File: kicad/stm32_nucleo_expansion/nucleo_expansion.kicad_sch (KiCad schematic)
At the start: 51 parts, among them CN10 NUCLE_F446RE_MORPHO_CN10, CN7 NUCLE_F446RE_MORPHO_CN7, J1 Conn_01x02_Male, J10 Conn_01x02_Male, J11 Conn_01x02_Male, J12 Conn_01x02_Male, J13 Conn_01x04_Male, J14 Conn_01x04_Male, J15 Conn_01x04_Male, J16 Conn_01x04_Male, J17 Conn_02x05_Counter_Clockwise, J18 Conn_01x02_Male, J19 Conn_01x02_Male, J2 Conn_01x02_Male, J20 Screw_Terminal_01x02, J21 Conn_02x05_Counter_Clockwise, J22 Conn_01x02_Male, J23 Screw_Terminal_01x02, J24 Screw_Terminal_01x02, J25 Micro_SD_Card_Det_Hirose_DM3AT, J26 Conn_01x02_Male, J27 Conn_01x03_Male, J28 Conn_01x03_Male, J29 Conn_01x03_Male, J3 Conn_01x02_Male, J32 Conn_01x02_Male, J4 Conn_01x02_Male, J5 Conn_01x02_Male, J6 Conn_01x02_Male, J7 Conn_01x02_Male, J8 Conn_01x02_Male, J9 Conn_01x02_Male, Q2 P30N06LE, Q3 P30N06LE

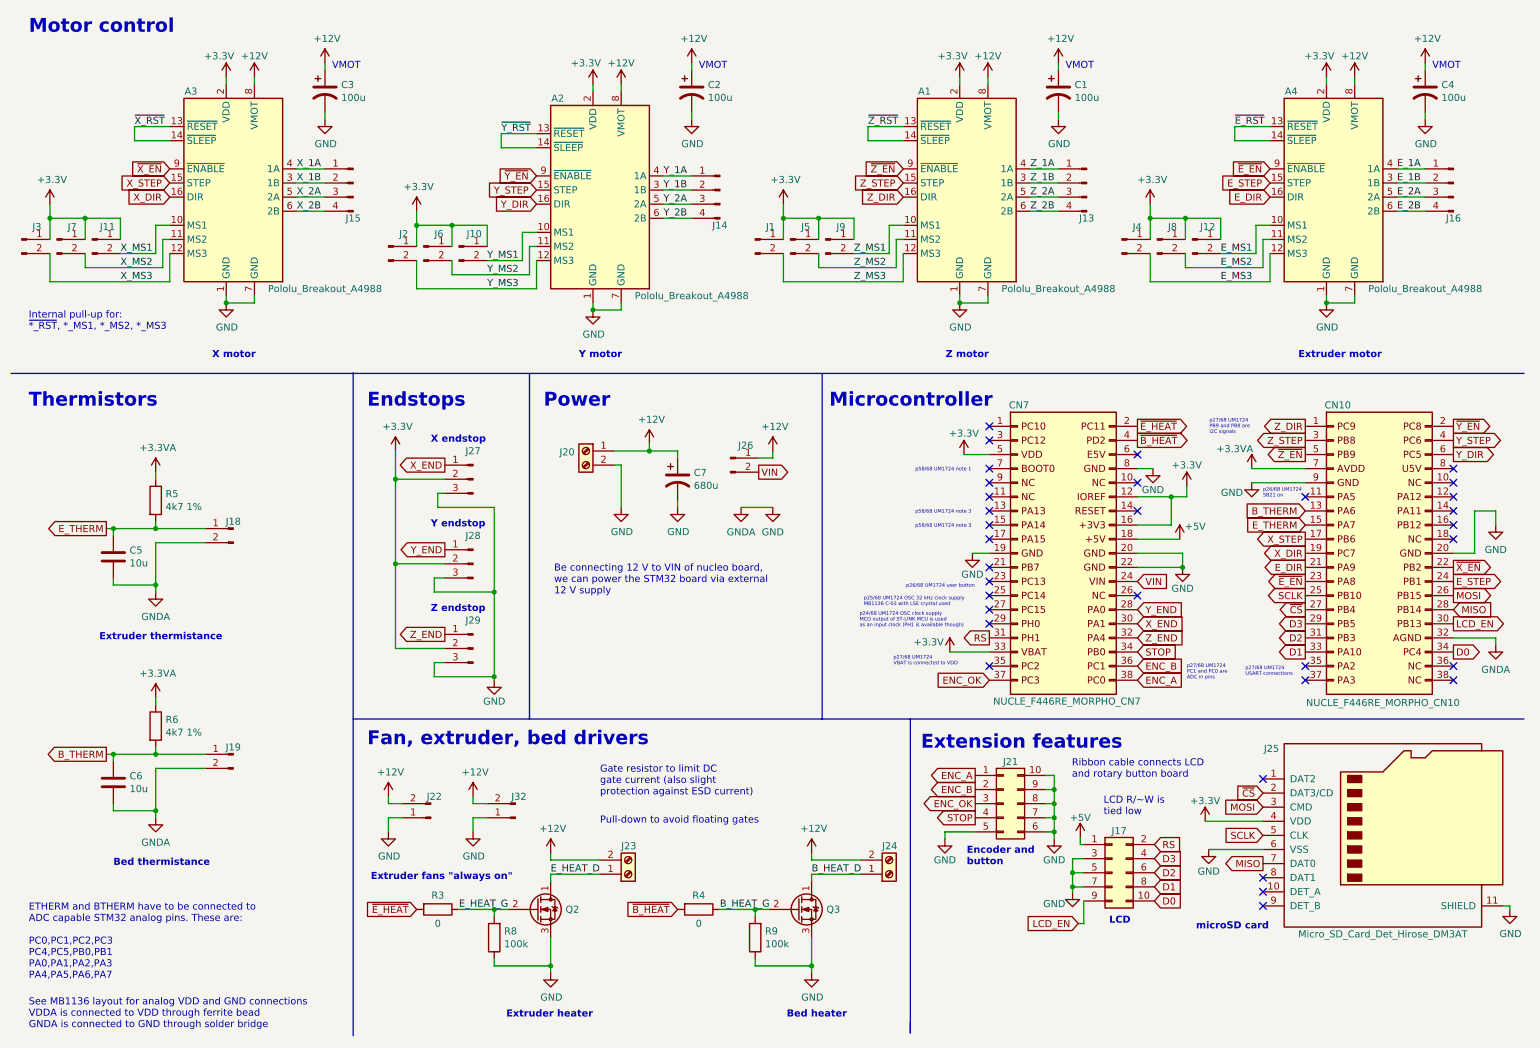
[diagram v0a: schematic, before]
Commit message: Clean up schematic and PCB
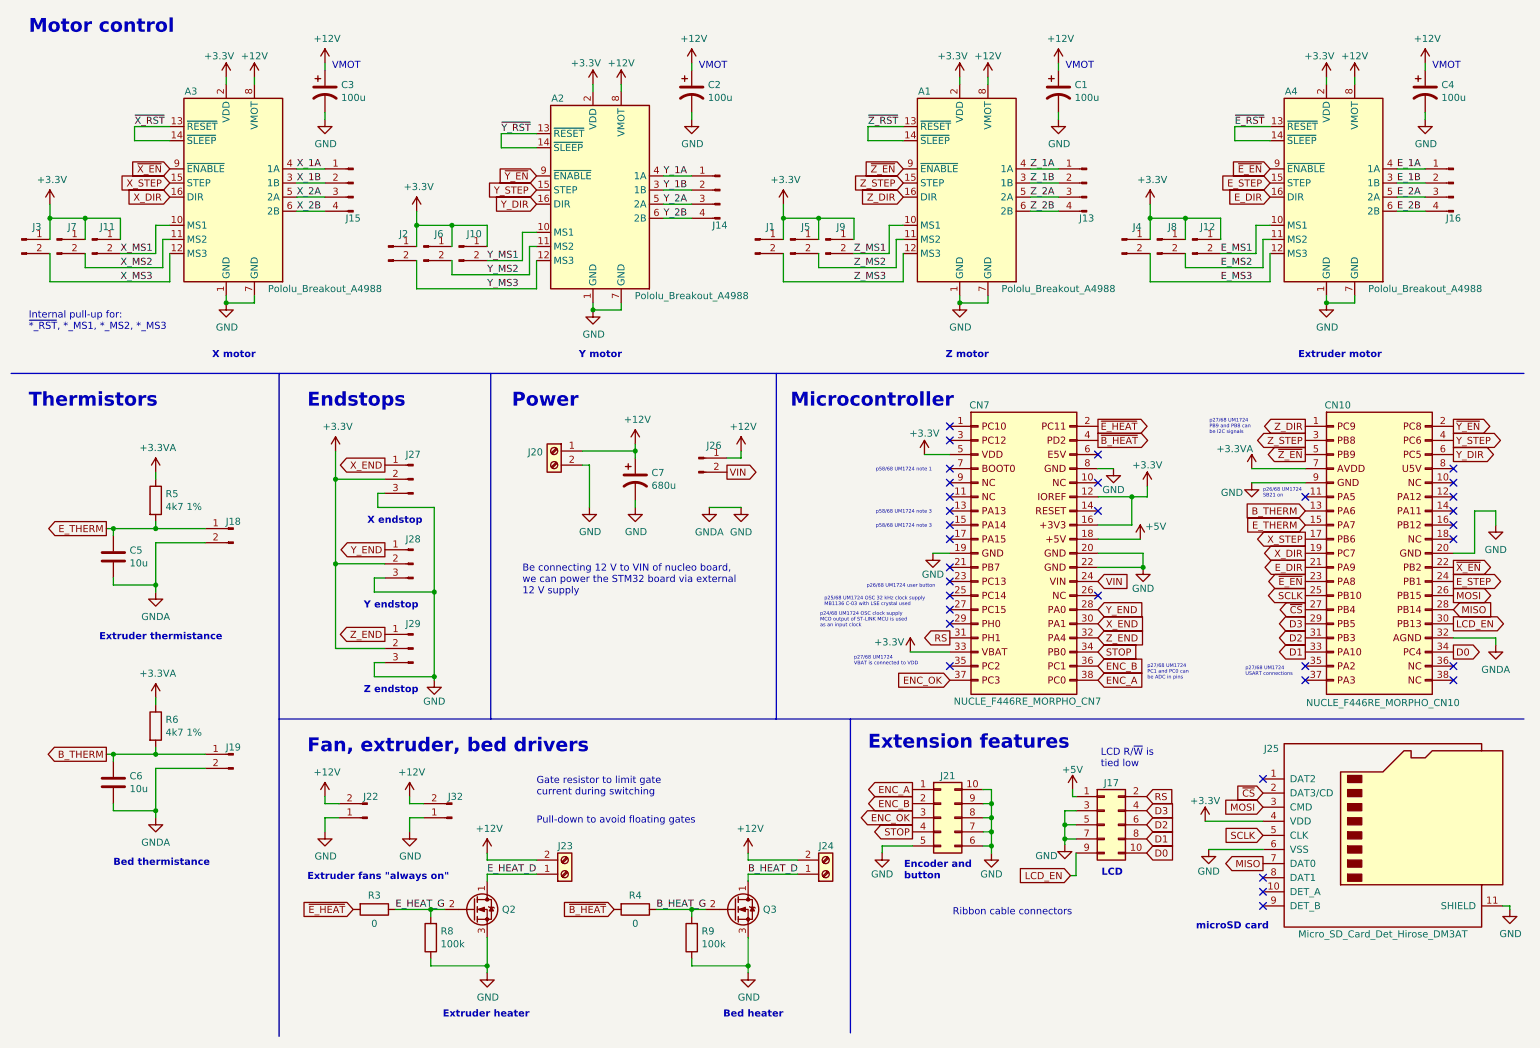
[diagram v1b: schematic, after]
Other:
- note added: "Gate resistor to limit gate current during switching"
- note added: "LCD R/~{W} is tied low"
- note added: "Ribbon cable connectors"
- note added: "p24/68 UM1724 OSC clock supply MCO output of ST-LINK MCU is used as an input clock"
- note added: "p27/68 UM1724 PB9 and PB8 can be I2C signals"
- note added: "p27/68 UM1724 PC1 and PC0 can be ADC in pins"
- note removed: "ETHERM and BTHERM have to be connected to ADC capable STM32 analog pins. These are: PC0,PC1,PC2,PC3 PC4,PC5,PB0,PB1 PA0,PA1,PA2,PA3 PA4,PA5,PA6,PA7"
- note removed: "Gate resistor to limit DC gate current (also slight protection against ESD current)"
- note removed: "LCD R/~W is tied low"
- note removed: "Ribbon cable connects LCD and rotary button board"
- note removed: "See MB1136 layout for analog VDD and GND connections VDDA is connected to VDD through ferrite bead GNDA is connected to GND through solder bridge"
- note removed: "p24/68 UM1724 OSC clock supply MCO output of ST-LINK MCU is used as an input clock (PH1 is available though)"
- note removed: "p27/68 UM1724 PB9 and PB8 are I2C signals"
- note removed: "p27/68 UM1724 PC1 and PC0 are ADC in pins"
- moved on the sheet: C7, CN7, J17, J20, J21, J22, J23, J24, J26, J27, J28, J29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

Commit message: Update schematic, PCB, and README (fab send-off v1.0)
SCHEMATIC:
- Clean up, rearrange some parts of the schematic
- Replace one of the "always on" fans with a PWM control using a BJT (BD237)
- Add fuses for fans
- Add fuse for main power (SMT fuse blade holder)
- Add fuse for extruder
- Add fuse for bed heater
- Add GPIO series resistors for off-board ribbon connections (ESD)
- Add microSD card decoupling capacitors
- Add decoupling capacitor for Pololu logic supply (3.3 V)
- Choose parts for NMOS drivers (original Teensylu MOSFETs)
- Choose gate resistors for NMOS (100 ohms)
- Add green status LED to free STM32 pin
- Add testpoints for microSD card detect pins
- Bring out 3.3 V on ribbon cable connector (J21)
- Rearrange encoder and button signals on CN7 for better routing
- Fix pin ordering for NMOS
- Fix pololu breakout motor connections (mimic original Teensylu connections)
- Fix microSD part name (DM3D)

PCB:
- Convert originally CNC fabrication board into a JLCPCB one
- Add QR code to this GitHub page on silkscreen layer
- Add informative text throughout board (labels, warnings, etc.)
- Incorporate schematic changes
- Reroute a few sections of the board
- Increase trace widths in certain places
- Add GND test points
- Increase spacing between ribbon cable connectors (so that the mating cables fit)
- Connect all nets (like GND and 3.3 V) to clear DRC errors
- Add 3D models for motor drivers and screw terminal blocks
- Create footprint for blade fuse holder
- Add JLCPCB order number on silkscreen
- Update gerbers (for JLCPCB fabrication)
- Fix orientation of capacitors underneath motor drivers
- Fix library footprints

README:
- Add preliminary power usage information
- Add to acknowledgements section

OTHER:
- Add bill of materials (BOM) -> parts ordered on DigiKey
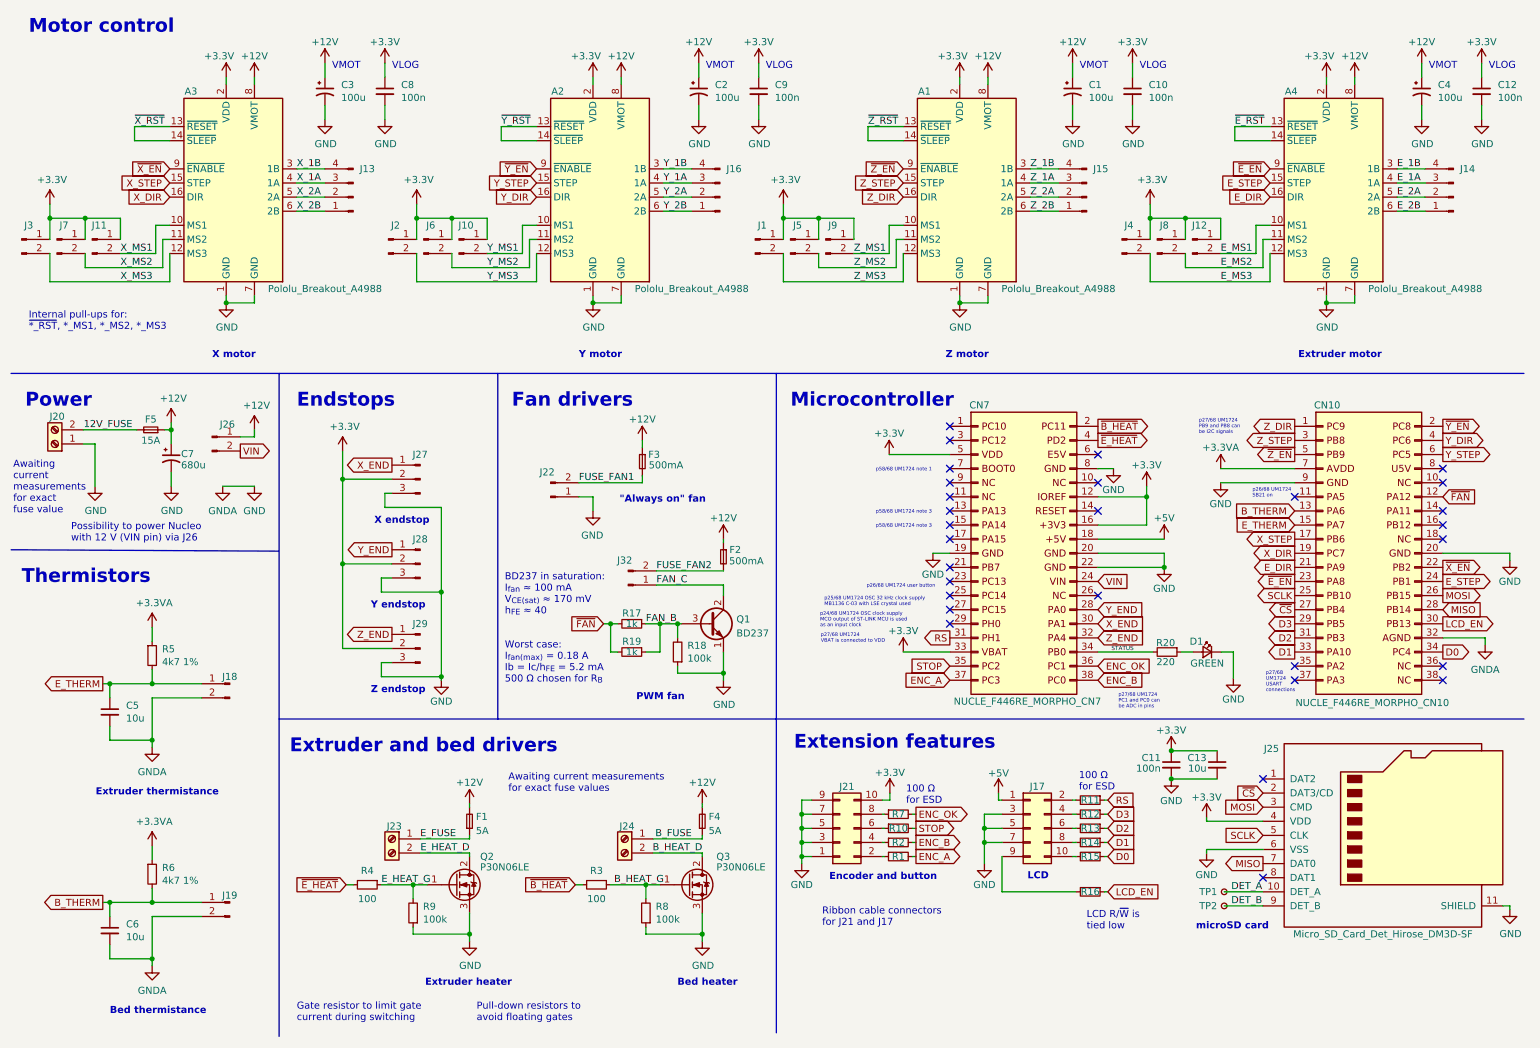
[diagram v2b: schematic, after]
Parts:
- removed C1, C2, C4: 100u, Capacitor_THT:CP_Radial_D5.0mm_P2.00mm, symbol Device:C_Polarized_US
- added C1, C2, C4: 100u, Capacitor_THT:CP_Radial_D5.0mm_P2.00mm, symbol Device:C_Polarized_Small_US
- added C10, C11, C12, C8, C9: 100n, Capacitor_SMD:C_0805_2012Metric_Pad1.18x1.45mm_HandSolder, symbol Device:C_Small
- added C13: 10u, Capacitor_SMD:C_0805_2012Metric_Pad1.18x1.45mm_HandSolder, symbol Device:C_Small
- added D1: GREEN, LED_THT:LED_D3.0mm, symbol Device:LED_Small
- added F1, F4: 5A, Fuse:Fuse_0603_1608Metric_Pad1.05x0.95mm_HandSolder, symbol Device:Fuse_Small
- added F2, F3: 500mA, Fuse:Fuse_0603_1608Metric_Pad1.05x0.95mm_HandSolder, symbol Device:Fuse_Small
- added F5: 15A, fuse:3586_mini, symbol Device:Fuse_Small
- added Q1: BD237, Package_TO_SOT_THT:TO-126-3_Vertical, symbol Transistor_BJT:BD237
- added R1, R10, R11, R12, R13, R14, R15, R16, R2, R7: 100, Resistor_SMD:R_0805_2012Metric_Pad1.20x1.40mm_HandSolder, symbol Device:R_Small
- added R17, R19: 1k, Resistor_SMD:R_0805_2012Metric_Pad1.20x1.40mm_HandSolder, symbol Device:R_Small
- added R18: 100k, Resistor_SMD:R_0805_2012Metric_Pad1.20x1.40mm_HandSolder, symbol Device:R_Small
- added R20: 220, Resistor_SMD:R_0805_2012Metric_Pad1.20x1.40mm_HandSolder, symbol Device:R_Small
- added TP1, TP2: TestPoint_Small, TestPoint:TestPoint_Pad_D1.0mm, symbol Connector:TestPoint_Small
- A1, A2, A3, A4: footprint Module:Pololu_Breakout-16_15.2x20.3mm -> pololu:Pololu_Breakout-16_15.2x20.3mm; symbol driver_motor_pololu:Pololu_Breakout_A4988 -> Driver_Motor:Pololu_Breakout_A4988; Product (none) -> STEPPER-DRIVER-STEPSTICKS-A4988
- C3: symbol Device:C_Polarized_US -> Device:C_Polarized_Small_US; DigiKey ID (none) -> 399-6102-ND; Product (none) -> ESK107M025AC3AA
- C5, C6: symbol Device:C -> Device:C_Small; DigiKey ID (none) -> 1276-1096-1-ND; Product (none) -> CL21A106KOQNNNE
- C7: symbol Device:C_Polarized_US -> Device:C_Polarized_Small_US; DigiKey ID (none) -> 732-8638-1-ND; Product (none) -> 860010475015
- CN10, CN7: DigiKey ID (none) -> S7122-ND; Product (none) -> PPPC192LFBN-RC
- J13, J14, J15, J16: DigiKey ID (none) -> WM19478-ND; Product (none) -> 0022280040
- J20, J23, J24: DigiKey ID (none) -> 732-10955-ND; Product (none) -> 691137710002
- J21: symbol Connector_Generic:Conn_02x05_Counter_Clockwise -> Connector_Generic:Conn_02x05_Odd_Even
- J22, J32: DigiKey ID (none) -> WM19485-ND; Product (none) -> 0022281020
- J25: value Micro_SD_Card_Det_Hirose_DM3AT -> Micro_SD_Card_Det_Hirose_DM3D-SF; DigiKey ID (none) -> H126097CT-ND; Product (none) -> DM3D-SF(41)
- J27, J28, J29: DigiKey ID (none) -> WM2792-ND; Product (none) -> 0022280030
- Q2, Q3: symbol Device:Q_NMOS_DGS -> Device:Q_NMOS_GDS; Product (none) -> P30N06LE
- R3: renamed from R4; value 0 -> 100; symbol Device:R -> Device:R_Small; DigiKey ID (none) -> RHM100KCT-ND; Product (none) -> ESR10EZPJ101
- R4: renamed from R3; value 0 -> 100; symbol Device:R -> Device:R_Small; DigiKey ID (none) -> RHM100KCT-ND; Product (none) -> ESR10EZPJ101
- R5, R6: symbol Device:R -> Device:R_Small; DigiKey ID (none) -> A129546CT-ND; Product (none) -> CRGH0805F4K7
- R8: renamed from R9; symbol Device:R -> Device:R_Small; DigiKey ID (none) -> RHM100KKCT-ND; Product (none) -> ESR10EZPJ104
- R9: renamed from R8; symbol Device:R -> Device:R_Small; DigiKey ID (none) -> RHM100KKCT-ND; Product (none) -> ESR10EZPJ104
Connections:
- net +12V: now also C1.1, C2.1, C4.1, F1.2, F2.1, F3.1, F4.2, F5.1; no longer J20.1 (Pin_1), J22.2 (Pin_2), J23.2 (Pin_2), J24.2 (Pin_2), J32.2 (Pin_2)
- net +3V3: now also J21.10 (Pin_10), C10.1, C11.1, C12.1, C13.1, C8.1, C9.1
- net B_HEAT_D: now also J24.2 (Pin_2), Q3.2 (D); no longer J24.1 (Pin_1), Q3.1 (D)
- net B_HEAT_G: now also Q3.1 (G); no longer Q3.2 (G)
- net D0: now also R15.1; no longer J17.10 (Pin_10)
- net D1: now also R14.1; no longer J17.8 (Pin_8)
- net D2: now also R13.1; no longer J17.6 (Pin_6)
- net D3: now also R12.1; no longer J17.4 (Pin_4)
- net ENC_A: now also CN7.37 (Pin_37), R1.2; no longer CN7.38 (Pin_38), J21.1 (Pin_1)
- net ENC_B: now also CN7.38 (Pin_38), R2.2; no longer CN7.36 (Pin_36), J21.2 (Pin_2)
- net ENC_OK: now also CN7.36 (Pin_36), R7.2; no longer CN7.37 (Pin_37), J21.3 (Pin_3)
- net E_1A: now also J14.3 (Pin_3); no longer J16.1 (Pin_1)
- net E_1B: now also J14.4 (Pin_4); no longer J16.2 (Pin_2)
- net E_2A: now also J14.2 (Pin_2); no longer J16.3 (Pin_3)
- net E_2B: now also J14.1 (Pin_1); no longer J16.4 (Pin_4)
- net E_HEAT_D: now also J23.2 (Pin_2), Q2.2 (D); no longer J23.1 (Pin_1), Q2.1 (D)
- net E_HEAT_G: now also Q2.1 (G); no longer Q2.2 (G)
- net GND: now also J20.1 (Pin_1), J21.1 (Pin_1), J21.3 (Pin_3), C1.2, C10.2, C11.2, C12.2, C13.2, C2.2, C4.2, C8.2, C9.2, D1.1 (K), Q1.1 (E), R18.1; no longer J20.2 (Pin_2), J21.10 (Pin_10), J21.6 (Pin_6), J21.8 (Pin_8), J32.1 (Pin_1)
- net LCD_EN: now also R16.1; no longer J17.9 (Pin_9)
- net RS: now also R11.1; no longer J17.2 (Pin_2)
- net STOP: now also CN7.35 (Pin_35), R10.2; no longer CN7.34 (Pin_34), J21.4 (Pin_4)
- net X_1A: now also J13.3 (Pin_3); no longer J15.1 (Pin_1)
- net X_1B: now also J13.4 (Pin_4); no longer J15.2 (Pin_2)
- net X_2A: now also J13.2 (Pin_2); no longer J15.3 (Pin_3)
- net X_2B: now also J13.1 (Pin_1); no longer J15.4 (Pin_4)
- net Y_1A: now also J16.3 (Pin_3); no longer J14.1 (Pin_1)
- net Y_1B: now also J16.4 (Pin_4); no longer J14.2 (Pin_2)
- net Y_2A: now also J16.2 (Pin_2); no longer J14.3 (Pin_3)
- net Y_2B: now also J16.1 (Pin_1); no longer J14.4 (Pin_4)
- net Y_DIR: now also CN10.4 (Pin_4); no longer CN10.6 (Pin_6)
- net Y_STEP: now also CN10.6 (Pin_6); no longer CN10.4 (Pin_4)
- net Z_1A: now also J15.3 (Pin_3); no longer J13.1 (Pin_1)
- net Z_1B: now also J15.4 (Pin_4); no longer J13.2 (Pin_2)
- net Z_2A: now also J15.2 (Pin_2); no longer J13.3 (Pin_3)
- net Z_2B: now also J15.1 (Pin_1); no longer J13.4 (Pin_4)
- net ~{B_HEAT}: now also CN7.2 (Pin_2); no longer CN7.4 (Pin_4)
- net ~{E_HEAT}: now also CN7.4 (Pin_4); no longer CN7.2 (Pin_2)
- net DET_A: now reaches J25.10 (DET_A)
- net DET_A: now also TP1.1
- net DET_B: now reaches J25.9 (DET_B)
- net DET_B: now also TP2.1
- net ~{FAN}: now reaches CN10.12 (Pin_12)
- net ~{FAN}: now also R17.2, R19.2
- new net: D1.2 (A), R20.1
- new net: J21.2 (Pin_2), R1.1
- new net: J21.4 (Pin_4), R2.1
- new net: J21.6 (Pin_6), R10.1
- new net: J21.8 (Pin_8), R7.1
- new net: J17.8 (Pin_8), R14.2
- new net: J17.10 (Pin_10), R15.2
- new net: J17.2 (Pin_2), R11.2
- new net: J17.4 (Pin_4), R12.2
- new net: J17.6 (Pin_6), R13.2
- new net: J17.9 (Pin_9), R16.2
- new net 12V_FUSE: F5.2, J20.2 (Pin_2)
- new net B_FUSE: F4.1, J24.1 (Pin_1)
- new net E_FUSE: F1.1, J23.1 (Pin_1)
- new net FAN_B: Q1.3 (B), R17.1, R18.2, R19.1
- new net FAN_C: J32.1 (Pin_1), Q1.2 (C)
- new net FUSE_FAN1: F3.2, J22.2 (Pin_2)
- new net FUSE_FAN2: F2.2, J32.2 (Pin_2)
- new net STATUS: CN7.34 (Pin_34), R20.2
- no-connect marks 33 -> 29
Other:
- note added: ""Always on" fan"
- note added: "100 Ω for ESD"
- note added: "Awaiting current measurements for exact fuse value"
- note added: "Awaiting current measurements for exact fuse values"
- note added: "BD237 in saturation: I_{fan} ≈ 100 mA V_{CE(sat)} ≈ 170 mV h_{FE} ≈ 40 Worst case: I_{fan(max)} = 0.18 A Ib = Ic/h_{FE} = 5.2 mA 500 Ω chosen for R_{B}"
- note added: "Extruder and bed drivers"
- note added: "Fan drivers"
- note added: "Internal pull-ups for: ~{*_RST}, *_MS1, *_MS2, *_MS3"
- note added: "PWM fan"
- note added: "Possibility to power Nucleo with 12 V (VIN pin) via J26"
- note added: "Pull-down resistors to avoid floating gates"
- note added: "Ribbon cable connectors for J21 and J17"
- note added: "VLOG"
- note removed: "Be connecting 12 V to VIN of nucleo board, we can power the STM32 board via external 12 V supply"
- note removed: "Extruder fans "always on""
- note removed: "Fan, extruder, bed drivers"
- note removed: "Internal pull-up for: ~{*_RST}, *_MS1, *_MS2, *_MS3"
- note removed: "Pull-down to avoid floating gates"
- note removed: "Ribbon cable connectors"
- moved on the sheet: A2, C5, C6, C7, CN10, J10, J13, J14, J15, J16, J17, J18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
